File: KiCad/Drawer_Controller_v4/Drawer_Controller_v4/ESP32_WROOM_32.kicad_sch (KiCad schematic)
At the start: 39 parts, among them Q1 SS8050, Q2 2N7002T-7-F, Q3 2N7002T-7-F, Q5 SS8050, U6 CP2102N-A02-GQFN28R, U7 ESP32-WROOM-32E-N8, X1 USB-Micro

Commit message: feat: completed `Drawer_Controller_v4`
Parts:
- renumbered C22 to C21, C21 to C22, C24 to C23, C29 to C24, C23 to C25, C25 to C26, C26 to C28, D7 to D3, F7 to F4, F6 to F5, F5 to F6, Q5 to Q6, Q1 to Q7, Q3 to Q8, Q2 to Q9, R25 to R24, R14 to R25, R15 to R26, R16 to R27, R21 to R28, R26 to R29, R18 to R30, R19 to R31, R17 to R32, R22 to R33, R23 to R34, R27 to R35, R20 to R36, R222 to R37, R221 to R38, R24 to R39, S1 to S2, S2 to S3, U6 to U5, U7 to U6, X1 to X7

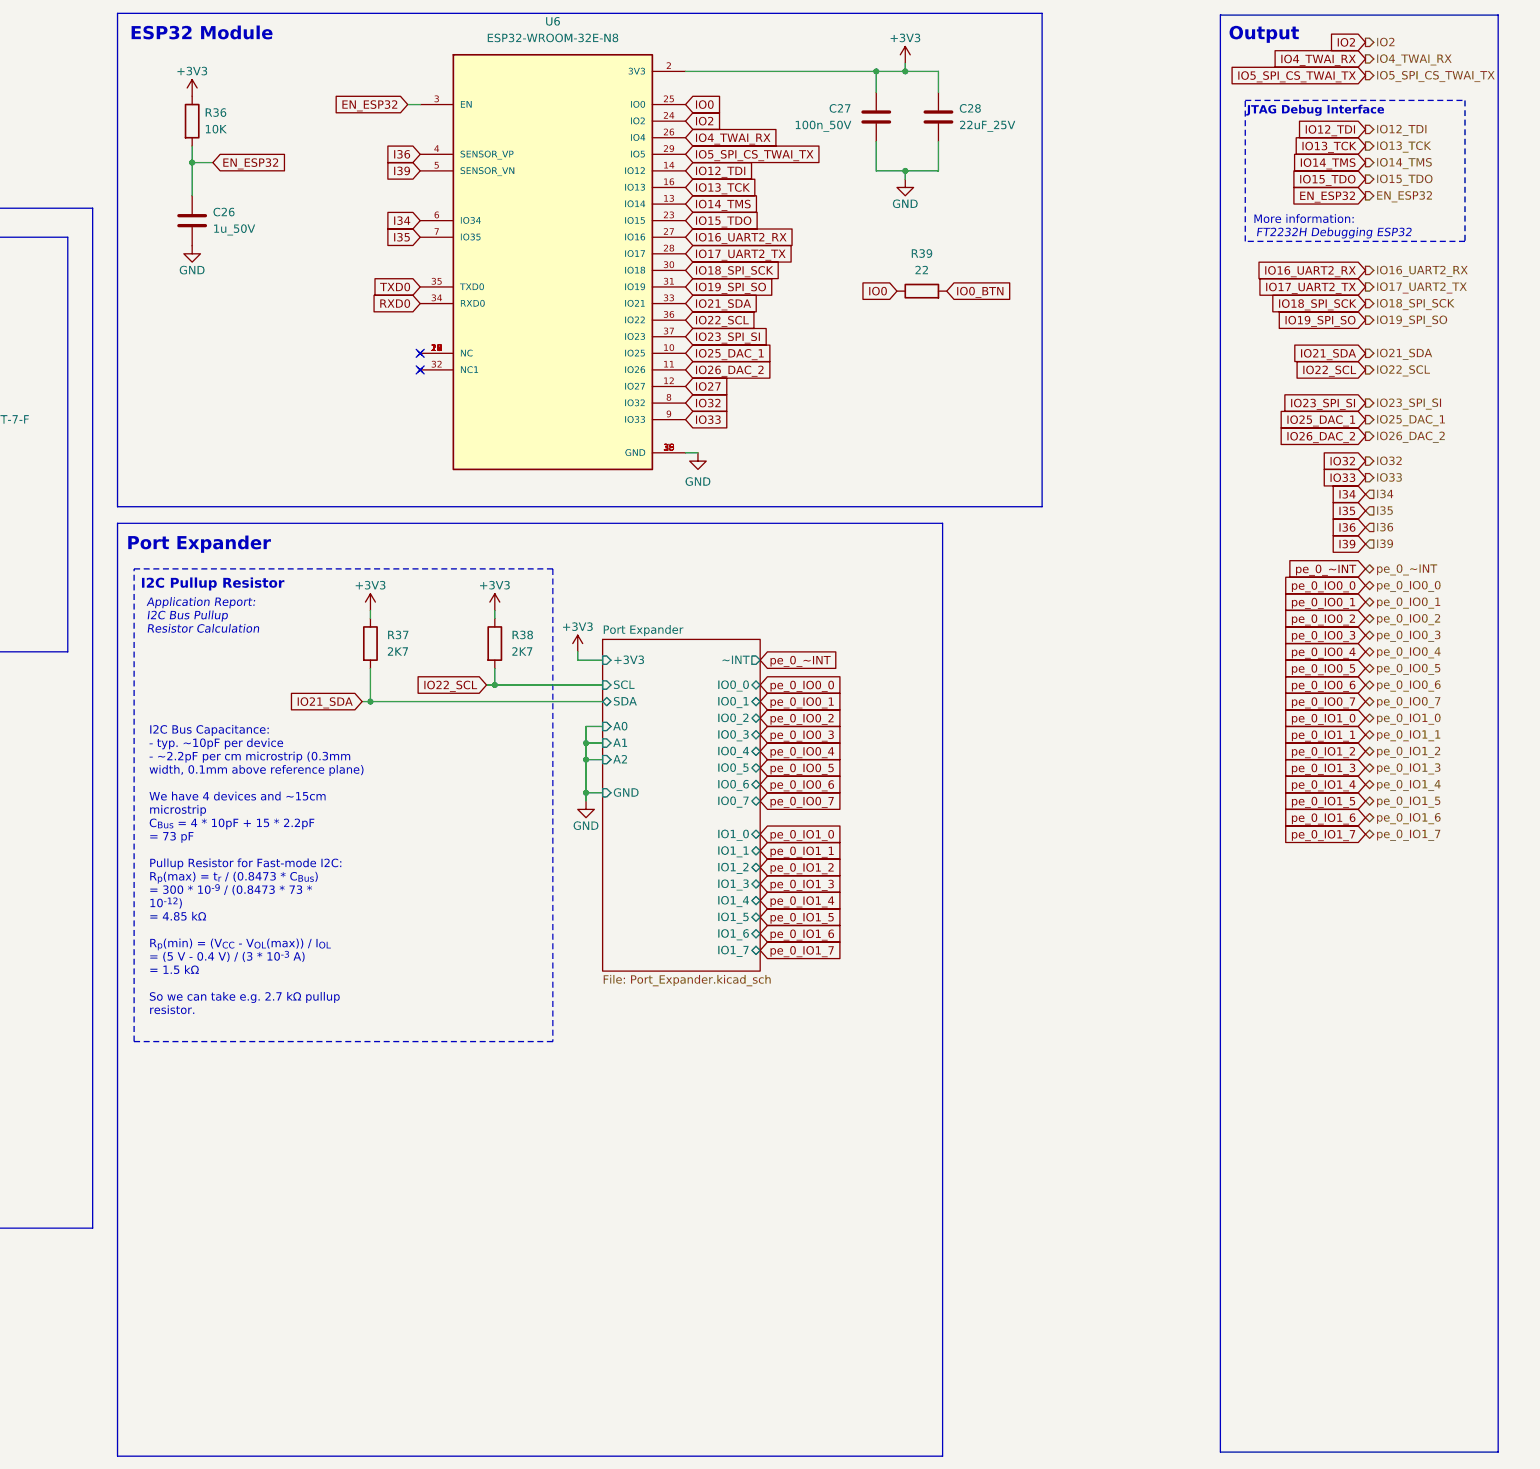
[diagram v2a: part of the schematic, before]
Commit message: feat: small final changes and creation of manufacturing files for `Drawer_Controller_v4`
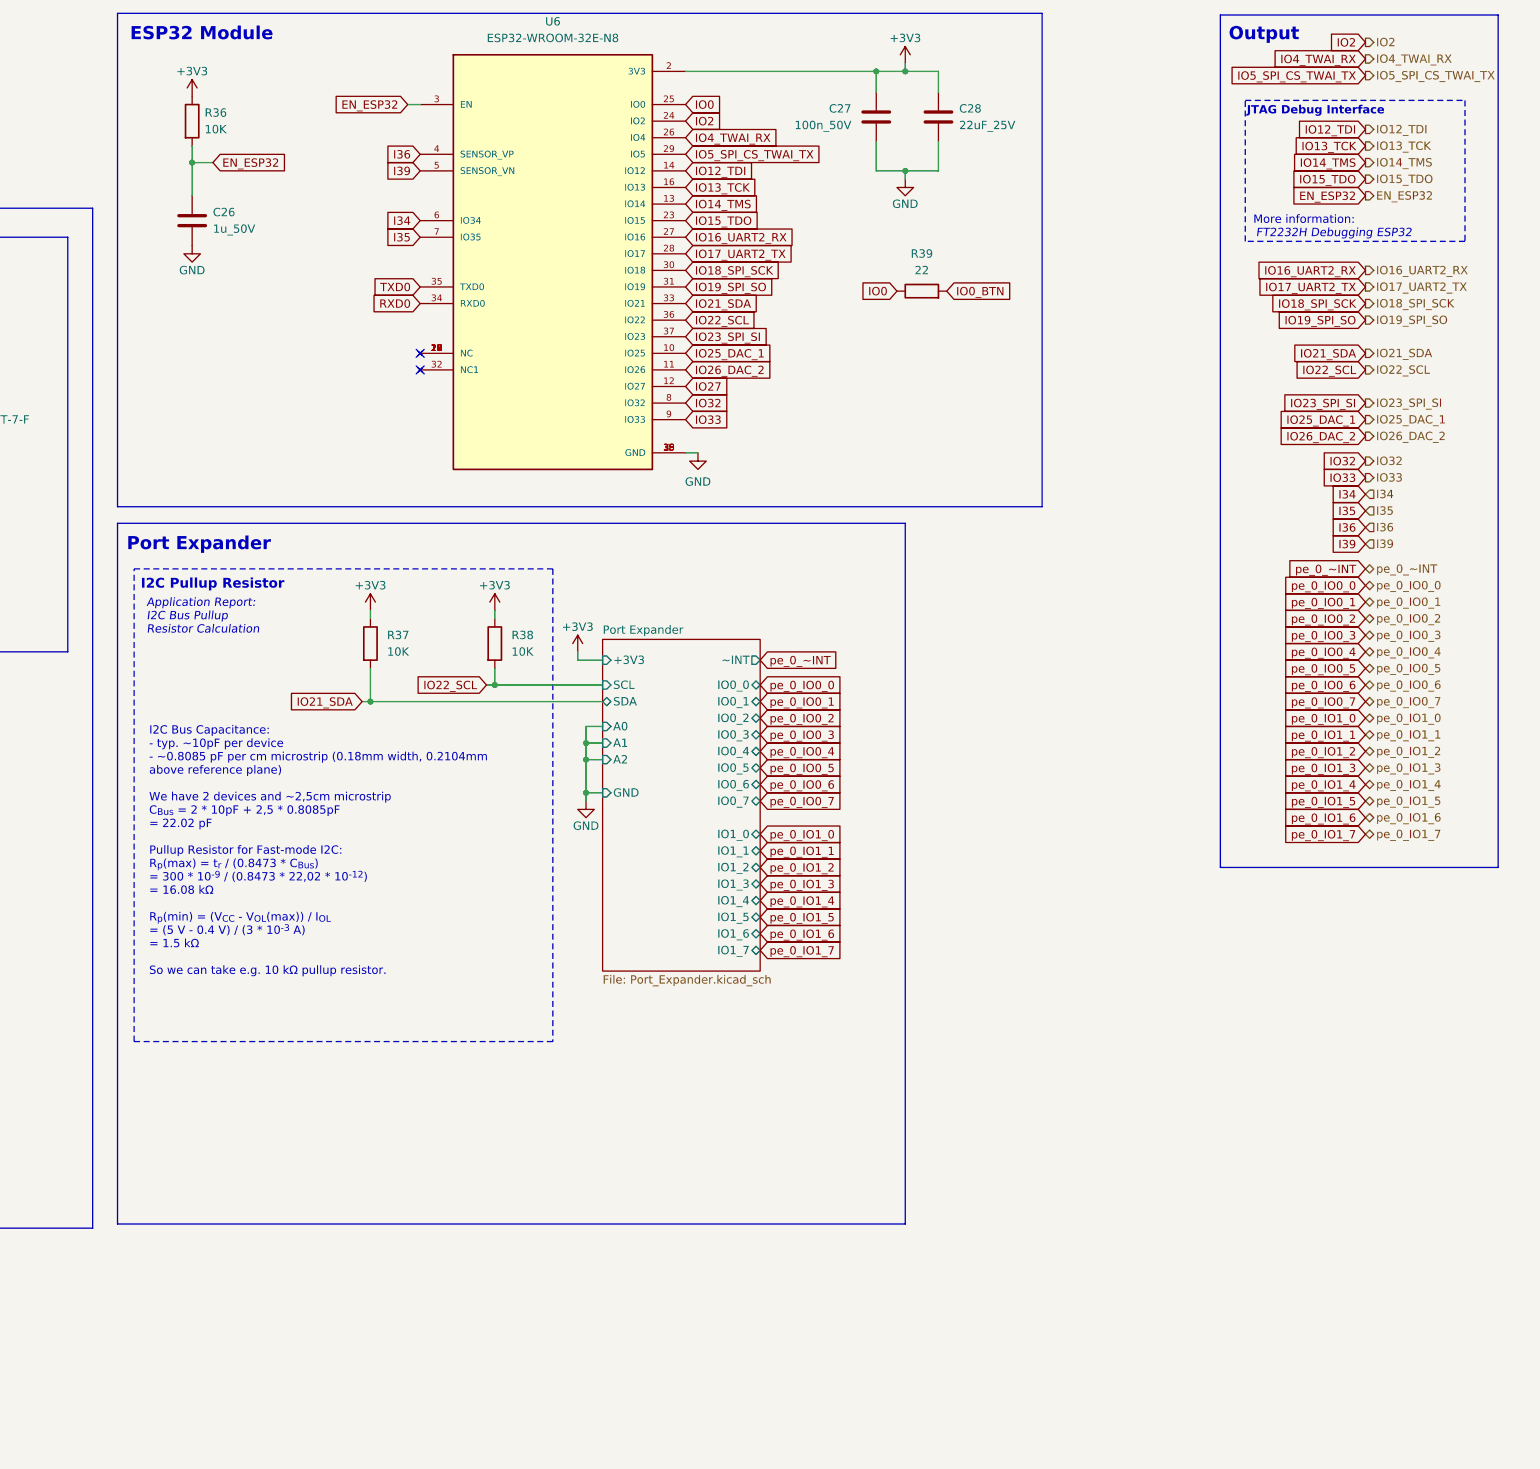
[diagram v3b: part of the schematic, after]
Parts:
- removed R37, R38: 2K7, Resistor_SMD:R_0603_1608Metric, symbol _R_0603:2K7
- added R37, R38: 10K, Resistor_SMD:R_0603_1608Metric, symbol _R_0603:10K
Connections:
- net +3V3: now also R37.1, R38.1
- net IO21_SDA: now also R37.2
- net IO22_SCL: now also R38.2
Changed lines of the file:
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@@
 	(rectangle
 		(start 193.675 92.075)
-		(end 320.04 234.95)
+		(end 314.325 199.39)
 		(stroke
 			(width 0)
@@
 	(rectangle
 		(start 362.585 14.224)
-		(end 405.13 234.315)
+		(end 405.13 144.78)
 		(stroke
 			(width 0)
@@
 		)
 	)
-	(text_box "I2C Bus Capacitance:\n- typ. ~10pF per device \n- ~2.2pF per cm microstrip (0.3mm width, 0.1mm above reference plane)\n\nWe have 4 devices and ~15cm microstrip\nC_{Bus} = 4 * 10pF + 15 * 2.2pF\n      = 73 pF\n\nPullup Resistor for Fast-mode I2C:\nR_{p}(max) = t_{r} / (0.8473 * C_{Bus})\n           = 300 * 10^{-9} / (0.8473 * 73 * 10^{-12})\n           = 4.85 kΩ\n\nR_{p}(min) = (V_{CC} - V_{OL}(max)) / I_{OL}\n           = (5 V - 0.4 V) / (3 * 10^{-3} A)\n           = 1.5 kΩ\n\nSo we can take e.g. 2.7 kΩ pullup resistor."
+	(text_box "I2C Bus Capacitance:\n- typ. ~10pF per device \n- ~0.8085 pF per cm microstrip (0.18mm width, 0.2104mm above reference plane)\n\nWe have 2 devices and ~2,5cm microstrip\nC_{Bus} = 2 * 10pF + 2,5 * 0.8085pF\n      = 22.02 pF\n\nPullup Resistor for Fast-mode I2C:\nR_{p}(max) = t_{r} / (0.8473 * C_{Bus})\n           = 300 * 10^{-9} / (0.8473 * 22,02 * 10^{-12})\n           = 16.08 kΩ\n\nR_{p}(min) = (V_{CC} - V_{OL}(max)) / I_{OL}\n           = (5 V - 0.4 V) / (3 * 10^{-3} A)\n           = 1.5 kΩ\n\nSo we can take e.g. 10 kΩ pullup resistor."
 		(exclude_from_sim no)
 		(at 197.485 121.92 0)
-		(size 40.64 42.291)
+		(size 60.96 46.355)
 		(stroke
 			(width -0.0001)
@@
 	)
 	(symbol
-		(lib_id "_R_0603:2K7")
-		(at 232.41 110.49 0)
-		(unit 1)
-		(exclude_from_sim no)
-		(in_bom yes)
-		(on_board yes)
-		(dnp no)
-		(fields_autoplaced yes)
-		(property "Reference" "R37"
-			(at 234.95 109.2199 0)
-			(effects
-				(font
-					(size 1.27 1.27)
-				)
-				(justify left)
-			)
-		)
-		(property "Value" "2K7"
-			(at 234.95 111.7599 0)
-			(effects
-				(font
-					(size 1.27 1.27)
-				)
-				(justify left)
-			)
-		)
-		(property "Footprint" "Resistor_SMD:R_0603_1608Metric"
-			(at 230.632 110.49 90)
-			(effects
-				(font
-					(size 1.27 1.27)
-				)
-				(hide yes)
-			)
-		)
-		(property "Datasheet" "~"
-			(at 232.41 110.49 0)
-			(effects
-				(font
-					(size 1.27 1.27)
-				)
-				(hide yes)
-			)
-		)
-		(property "Description" "Resistor 2K7 1% 100mW 75V 0603"
-			(at 232.41 110.49 0)
-			(effects
-				(font
-					(size 1.27 1.27)
-				)
-				(hide yes)
-			)
-		)
-		(property "MF" "UNI-ROYAL"
-			(at 232.41 110.49 0)
-			(effects
-				(font
-					(size 1.27 1.27)
-				)
-				(hide yes)
-			)
-		)
-		(property "MPN" "0603WAF2701T5E"
-			(at 232.41 110.49 0)
-			(effects
-				(font
-					(size 1.27 1.27)
-				)
-				(hide yes)
-			)
-		)
-		(property "OC_LCSC" "C13167"
-			(at 232.41 110.49 0)
-			(effects
-				(font
-					(size 1.27 1.27)
-				)
-				(hide yes)
-			)
-		)
-		(property "OC_MOUSER" ""
-			(at 232.41 110.49 0)
-			(effects
-				(font
-					(size 1.27 1.27)
-				)
-				(hide yes)
-			)
-		)
-		(pin "2"
-		)
-		(pin "1"
-		)
-		(instances
-			(project "Drawer_Controller_v4"
-				(path "/57f8c193-fe09-43d3-9441-dbd40881d2aa/d19b84cd-4ee4-4d95-811d-38c072072447"
-					(reference "R37")
-					(unit 1)
-				)
-			)
-		)
-	)
-	(symbol
 		(lib_id "_C_0402:100n_50V")
 		(at 59.055 32.385 90)
@@
 	)
 	(symbol
+		(lib_id "_R_0603:10K")
+		(at 232.41 110.49 0)
+		(unit 1)
+		(exclude_from_sim no)
+		(in_bom yes)
+		(on_board yes)
+		(dnp no)
+		(fields_autoplaced yes)
+		(property "Reference" "R37"
+			(at 234.95 109.2199 0)
+			(effects
+				(font
+					(size 1.27 1.27)
+				)
+				(justify left)
+			)
+		)
+		(property "Value" "10K"
+			(at 234.95 111.7599 0)
+			(effects
+				(font
+					(size 1.27 1.27)
+				)
+				(justify left)
+			)
+		)
+		(property "Footprint" "Resistor_SMD:R_0603_1608Metric"
+			(at 230.632 110.49 90)
+			(effects
+				(font
+					(size 1.27 1.27)
+				)
+				(hide yes)
+			)
+		)
+		(property "Datasheet" "~"
+			(at 232.41 110.49 0)
+			(effects
+				(font
+					(size 1.27 1.27)
+				)
+				(hide yes)
+			)
+		)
+		(property "Description" "Resistor 10K 1% 100mW 75V 0603"
+			(at 232.41 110.49 0)
+			(effects
+				(font
+					(size 1.27 1.27)
+				)
+				(hide yes)
+			)
+		)
+		(property "MF" "UNI-ROYAL"
+			(at 232.41 110.49 0)
+			(effects
+				(font
+					(size 1.27 1.27)
+				)
+				(hide yes)
+			)
+		)
+		(property "MPN" "0603WAF1002T5E"
+			(at 232.41 110.49 0)
+			(effects
+				(font
+					(size 1.27 1.27)
+				)
+				(hide yes)
+			)
+		)
+		(property "OC_LCSC" "C25804"
+			(at 232.41 110.49 0)
+			(effects
+				(font
+					(size 1.27 1.27)
+				)
+				(hide yes)
+			)
+		)
+		(property "OC_MOUSER" ""
+			(at 232.41 110.49 0)
+			(effects
+				(font
+					(size 1.27 1.27)
+				)
+				(hide yes)
+			)
+		)
+		(pin "2"
+		)
+		(pin "1"
+		)
+		(instances
+			(project "Drawer_Controller_v4"
+				(path "/57f8c193-fe09-43d3-9441-dbd40881d2aa/d19b84cd-4ee4-4d95-811d-38c072072447"
+					(reference "R37")
+					(unit 1)
+				)
+			)
+		)
+	)
+	(symbol
 		(lib_id "_Switch:TS-1187A-B-A-B")
 		(at 59.055 25.4 0)
@@
 	)
 	(symbol
-		(lib_id "_R_0603:2K7")
-		(at 251.46 110.49 0)
-		(unit 1)
-		(exclude_from_sim no)
-		(in_bom yes)
-		(on_board yes)
-		(dnp no)
-		(fields_autoplaced yes)
-		(property "Reference" "R38"
-			(at 254 109.2199 0)
-			(effects
-				(font
-					(size 1.27 1.27)
-				)
-				(justify left)
-			)
-		)
-		(property "Value" "2K7"
-			(at 254 111.7599 0)
-			(effects
-				(font
-					(size 1.27 1.27)
-				)
-				(justify left)
-			)
-		)
-		(property "Footprint" "Resistor_SMD:R_0603_1608Metric"
-			(at 249.682 110.49 90)
-			(effects
-				(font
-					(size 1.27 1.27)
-				)
-				(hide yes)
-			)
-		)
-		(property "Datasheet" "~"
-			(at 251.46 110.49 0)
-			(effects
-				(font
-					(size 1.27 1.27)
-				)
-				(hide yes)
-			)
-		)
-		(property "Description" "Resistor 2K7 1% 100mW 75V 0603"
-			(at 251.46 110.49 0)
-			(effects
-				(font
-					(size 1.27 1.27)
-				)
-				(hide yes)
-			)
-		)
-		(property "MF" "UNI-ROYAL"
-			(at 251.46 110.49 0)
-			(effects
-				(font
-					(size 1.27 1.27)
-				)
-				(hide yes)
-			)
-		)
-		(property "MPN" "0603WAF2701T5E"
-			(at 251.46 110.49 0)
-			(effects
-				(font
-					(size 1.27 1.27)
-				)
-				(hide yes)
-			)
-		)
-		(property "OC_LCSC" "C13167"
-			(at 251.46 110.49 0)
-			(effects
-				(font
-					(size 1.27 1.27)
-				)
-				(hide yes)
-			)
-		)
-		(property "OC_MOUSER" ""
-			(at 251.46 110.49 0)
-			(effects
-				(font
-					(size 1.27 1.27)
-				)
-				(hide yes)
-			)
-		)
-		(pin "2"
-		)
-		(pin "1"
-		)
-		(instances
-			(project "Drawer_Controller_v4"
-				(path "/57f8c193-fe09-43d3-9441-dbd40881d2aa/d19b84cd-4ee4-4d95-811d-38c072072447"
-					(reference "R38")
-					(unit 1)
-				)
-			)
-		)
-	)
-	(symbol
 		(lib_id "_R_0402:10K")
 		(at 35.56 121.92 90)
@@
 					(unit 1)
 				)
+			)
+		)
+	)
+	(symbol
+		(lib_id "_R_0603:10K")
+		(at 251.46 110.49 0)
+		(unit 1)
+		(exclude_from_sim no)
+		(in_bom yes)
+		(on_board yes)
+		(dnp no)
+		(fields_autoplaced yes)
+		(property "Reference" "R38"
+			(at 254 109.2199 0)
+			(effects
+				(font
+					(size 1.27 1.27)
+				)
+				(justify left)
+			)
+		)
+		(property "Value" "10K"
+			(at 254 111.7599 0)
+			(effects
+				(font
+					(size 1.27 1.27)
+				)
+				(justify left)
+			)
+		)
+		(property "Footprint" "Resistor_SMD:R_0603_1608Metric"
+			(at 249.682 110.49 90)
+			(effects
+				(font
+					(size 1.27 1.27)
+				)
+				(hide yes)
+			)
+		)
+		(property "Datasheet" "~"
+			(at 251.46 110.49 0)
+			(effects
+				(font
+					(size 1.27 1.27)
+				)
+				(hide yes)
+			)
+		)
+		(property "Description" "Resistor 10K 1% 100mW 75V 0603"
+			(at 251.46 110.49 0)
+			(effects
+				(font
+					(size 1.27 1.27)
+				)
+				(hide yes)
+			)
+		)
+		(property "MF" "UNI-ROYAL"
+			(at 251.46 110.49 0)
+			(effects
+				(font
+					(size 1.27 1.27)
+				)
+				(hide yes)
+			)
+		)
+		(property "MPN" "0603WAF1002T5E"
+			(at 251.46 110.49 0)
+			(effects
+				(font
+					(size 1.27 1.27)
+				)
+				(hide yes)
+			)
+		)
+		(property "OC_LCSC" "C25804"
+			(at 251.46 110.49 0)
+			(effects
+				(font
+					(size 1.27 1.27)
+				)
+				(hide yes)
+			)
+		)
+		(property "OC_MOUSER" ""
+			(at 251.46 110.49 0)
+			(effects
+				(font
+					(size 1.27 1.27)
+				)
+				(hide yes)
+			)
+		)
+		(pin "2"
+		)
+		(pin "1"
+		)
+		(instances
+			(project "Drawer_Controller_v4"
+				(path "/57f8c193-fe09-43d3-9441-dbd40881d2aa/d19b84cd-4ee4-4d95-811d-38c072072447"
+					(reference "R38")
+					(unit 1)
+				)
